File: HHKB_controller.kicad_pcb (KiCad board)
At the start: 2 copper layers, 141.5 x 36 mm, 95 parts, among them CN1 JP, CN2 PRO2, J1 USB_mini_micro_B, P1 GND, P10 CONN_1, P100 LIPO, P11 CONN_1, P110 CONN_1, P111 CONN_1, P112 CONN_1, P113 CONN_1, P114 CONN_1, P115 CONN_1, P12 CONN_1, P13 CONN_1, P14 CONN_1, P15 CONN_1, P2 D+, P3 D-, P4 VUSB, P5 PD1, P6 PD0, P7 GND, P8 CONN_3X2, P9 CONN_1, Q1 Nch, Q10 Nch, Q2 Nch, Q3 Nch, Q4 Pch, Q5 Pch, SW1 SW_PUSH, SW2 SW_DPDT, U1 ATMEGA32U4, U2 MIC5504-3.3YMTR, U3 NCP1402SN50, U4 MCP73832, U5 RN42, X1 16MHz

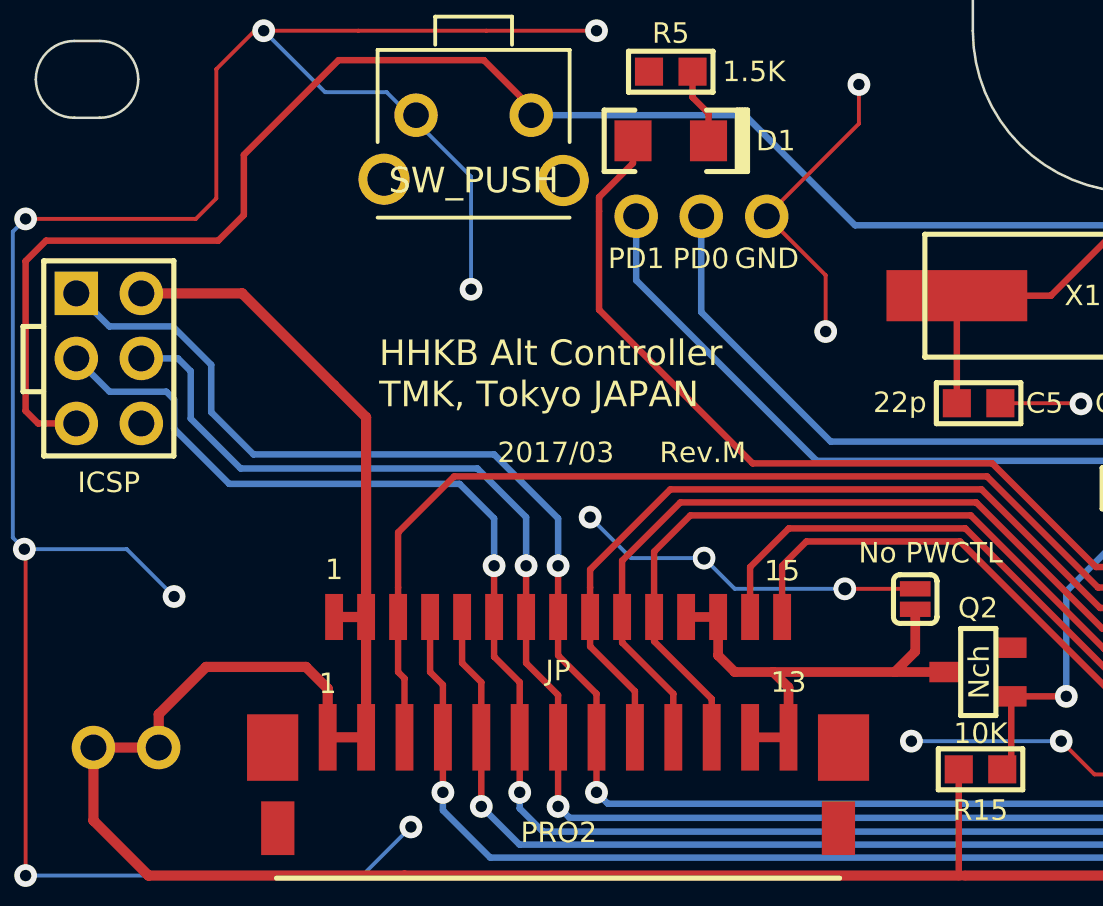
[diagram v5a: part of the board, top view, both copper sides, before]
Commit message: Fix footprints for HRS DF14 and SKHH
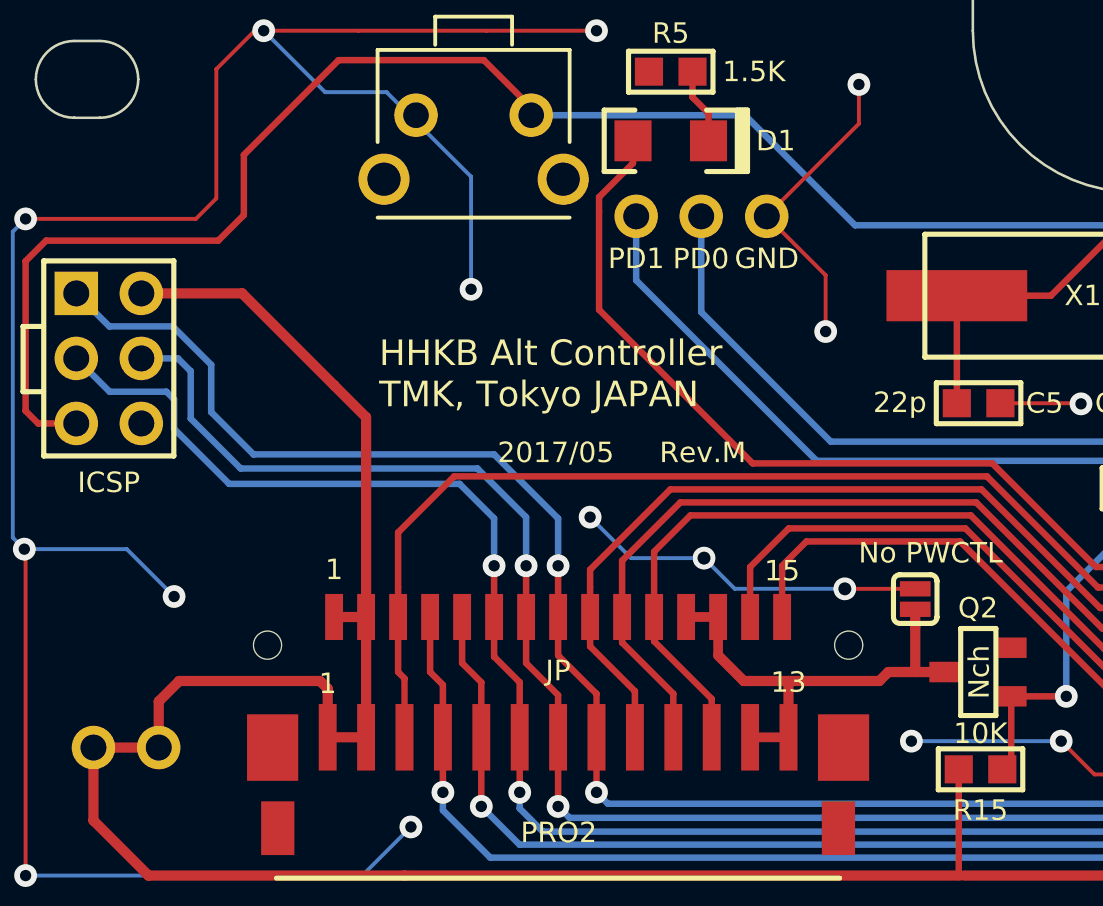
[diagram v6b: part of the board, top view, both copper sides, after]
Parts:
- CN1: footprint keyboard_parts:HHKB_JP_HRS_DF14_15P -> HHKB_JP_HRS_DF14_15P
- SW1: footprint keyboard_parts:SW_TACT_TH_HORIZ -> SW_TACT_TH_HORIZ
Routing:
- net /HHKB_GND: track 18.9 -> 18.3 mm
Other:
- board text added: "2017/05"
- board text removed: "2017/03"

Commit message: Fix USB footprint: add SMD pads for frame
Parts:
- G***: footprint keyboard_parts:tmk2016 -> keyboard_parts:tmk_logo
- J1: footprint USB_miniB_hirose_5S8 -> keyboard_parts:USB_miniB_hirose_5S8
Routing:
- net GND: track 464.7 -> 476.1 mm
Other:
- board text added: "2017/06"
- board text added: "Rev.N"
- board text removed: "2017/05"
- board text removed: "Rev.M"
